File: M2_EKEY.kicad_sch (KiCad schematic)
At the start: 36 parts, among them J2 Bus_M.2_Socket_E, J31 Bus_M.2_Socket_E, J34 Bus_M.2_Socket_E

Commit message: went back to the drawing board
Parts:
- C200, C201, C202, C203, C49, C50, J34, R142, R148, R149, R150: now not fitted

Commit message: some power stuff (unfinished)
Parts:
- C200, C201, C202, C203, C49, C50, J34, R142, R148, R149, R150: now fitted
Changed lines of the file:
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@@
 		(exclude_from_sim no)
 		(in_bom yes)
-		(on_board no)
+		(on_board yes)
 		(in_pos_files yes)
-		(dnp yes)
+		(dnp no)
 		(property "Reference" "C203"
 			(at 228.6 173.99 90)
@@
 		(exclude_from_sim no)
 		(in_bom yes)
-		(on_board no)
+		(on_board yes)
 		(in_pos_files yes)
-		(dnp yes)
+		(dnp no)
 		(fields_autoplaced yes)
 		(property "Reference" "#PWR0292"
@@
 		(exclude_from_sim no)
 		(in_bom yes)
-		(on_board no)
+		(on_board yes)
 		(in_pos_files yes)
-		(dnp yes)
+		(dnp no)
 		(fields_autoplaced yes)
 		(property "Reference" "#PWR0289"
@@
 		(exclude_from_sim no)
 		(in_bom yes)
-		(on_board no)
+		(on_board yes)
 		(in_pos_files yes)
-		(dnp yes)
+		(dnp no)
 		(property "Reference" "C201"
 			(at 228.6 161.29 90)
@@
 		(exclude_from_sim no)
 		(in_bom yes)
-		(on_board no)
+		(on_board yes)
 		(in_pos_files yes)
-		(dnp yes)
+		(dnp no)
 		(property "Reference" "C49"
 			(at 156.21 193.04 90)
@@
 		(exclude_from_sim no)
 		(in_bom yes)
-		(on_board no)
+		(on_board yes)
 		(in_pos_files yes)
-		(dnp yes)
+		(dnp no)
 		(property "Reference" "C200"
 			(at 228.6 154.94 90)
@@
 		(exclude_from_sim no)
 		(in_bom yes)
-		(on_board no)
+		(on_board yes)
 		(in_pos_files yes)
-		(dnp yes)
+		(dnp no)
 		(property "Reference" "R148"
 			(at 264.16 256.54 90)
@@
 		(exclude_from_sim no)
 		(in_bom yes)
-		(on_board no)
+		(on_board yes)
 		(in_pos_files yes)
-		(dnp yes)
+		(dnp no)
 		(property "Reference" "R149"
 			(at 257.81 201.93 0)
@@
 		(exclude_from_sim no)
 		(in_bom yes)
-		(on_board no)
+		(on_board yes)
 		(in_pos_files yes)
-		(dnp yes)
+		(dnp no)
 		(fields_autoplaced yes)
 		(property "Reference" "#PWR0298"
@@
 		(exclude_from_sim no)
 		(in_bom yes)
-		(on_board no)
+		(on_board yes)
 		(in_pos_files yes)
-		(dnp yes)
+		(dnp no)
 		(fields_autoplaced yes)
 		(property "Reference" "J34"
@@
 		(exclude_from_sim no)
 		(in_bom yes)
-		(on_board no)
+		(on_board yes)
 		(in_pos_files yes)
-		(dnp yes)
+		(dnp no)
 		(fields_autoplaced yes)
 		(property "Reference" "#PWR0290"
@@
 		(exclude_from_sim no)
 		(in_bom no)
-		(on_board no)
+		(on_board yes)
 		(in_pos_files yes)
 		(dnp yes)
@@
 		(exclude_from_sim no)
 		(in_bom yes)
-		(on_board no)
+		(on_board yes)
 		(in_pos_files yes)
-		(dnp yes)
+		(dnp no)
 		(property "Reference" "R142"
 			(at 191.77 167.64 0)
@@
 		(exclude_from_sim no)
 		(in_bom yes)
-		(on_board no)
+		(on_board yes)
 		(in_pos_files yes)
-		(dnp yes)
+		(dnp no)
 		(property "Reference" "R150"
 			(at 264.16 204.47 0)
@@
 		(exclude_from_sim no)
 		(in_bom yes)
-		(on_board no)
+		(on_board yes)
 		(in_pos_files yes)
-		(dnp yes)
+		(dnp no)
 		(fields_autoplaced yes)
 		(property "Reference" "#PWR0291"
@@
 		(exclude_from_sim no)
 		(in_bom yes)
-		(on_board no)
+		(on_board yes)
 		(in_pos_files yes)
-		(dnp yes)
+		(dnp no)
 		(property "Reference" "C50"
 			(at 156.21 195.58 90)
@@
 		(exclude_from_sim no)
 		(in_bom yes)
-		(on_board no)
+		(on_board yes)
 		(in_pos_files yes)
-		(dnp yes)
+		(dnp no)
 		(property "Reference" "C202"
 			(at 228.6 167.64 90)

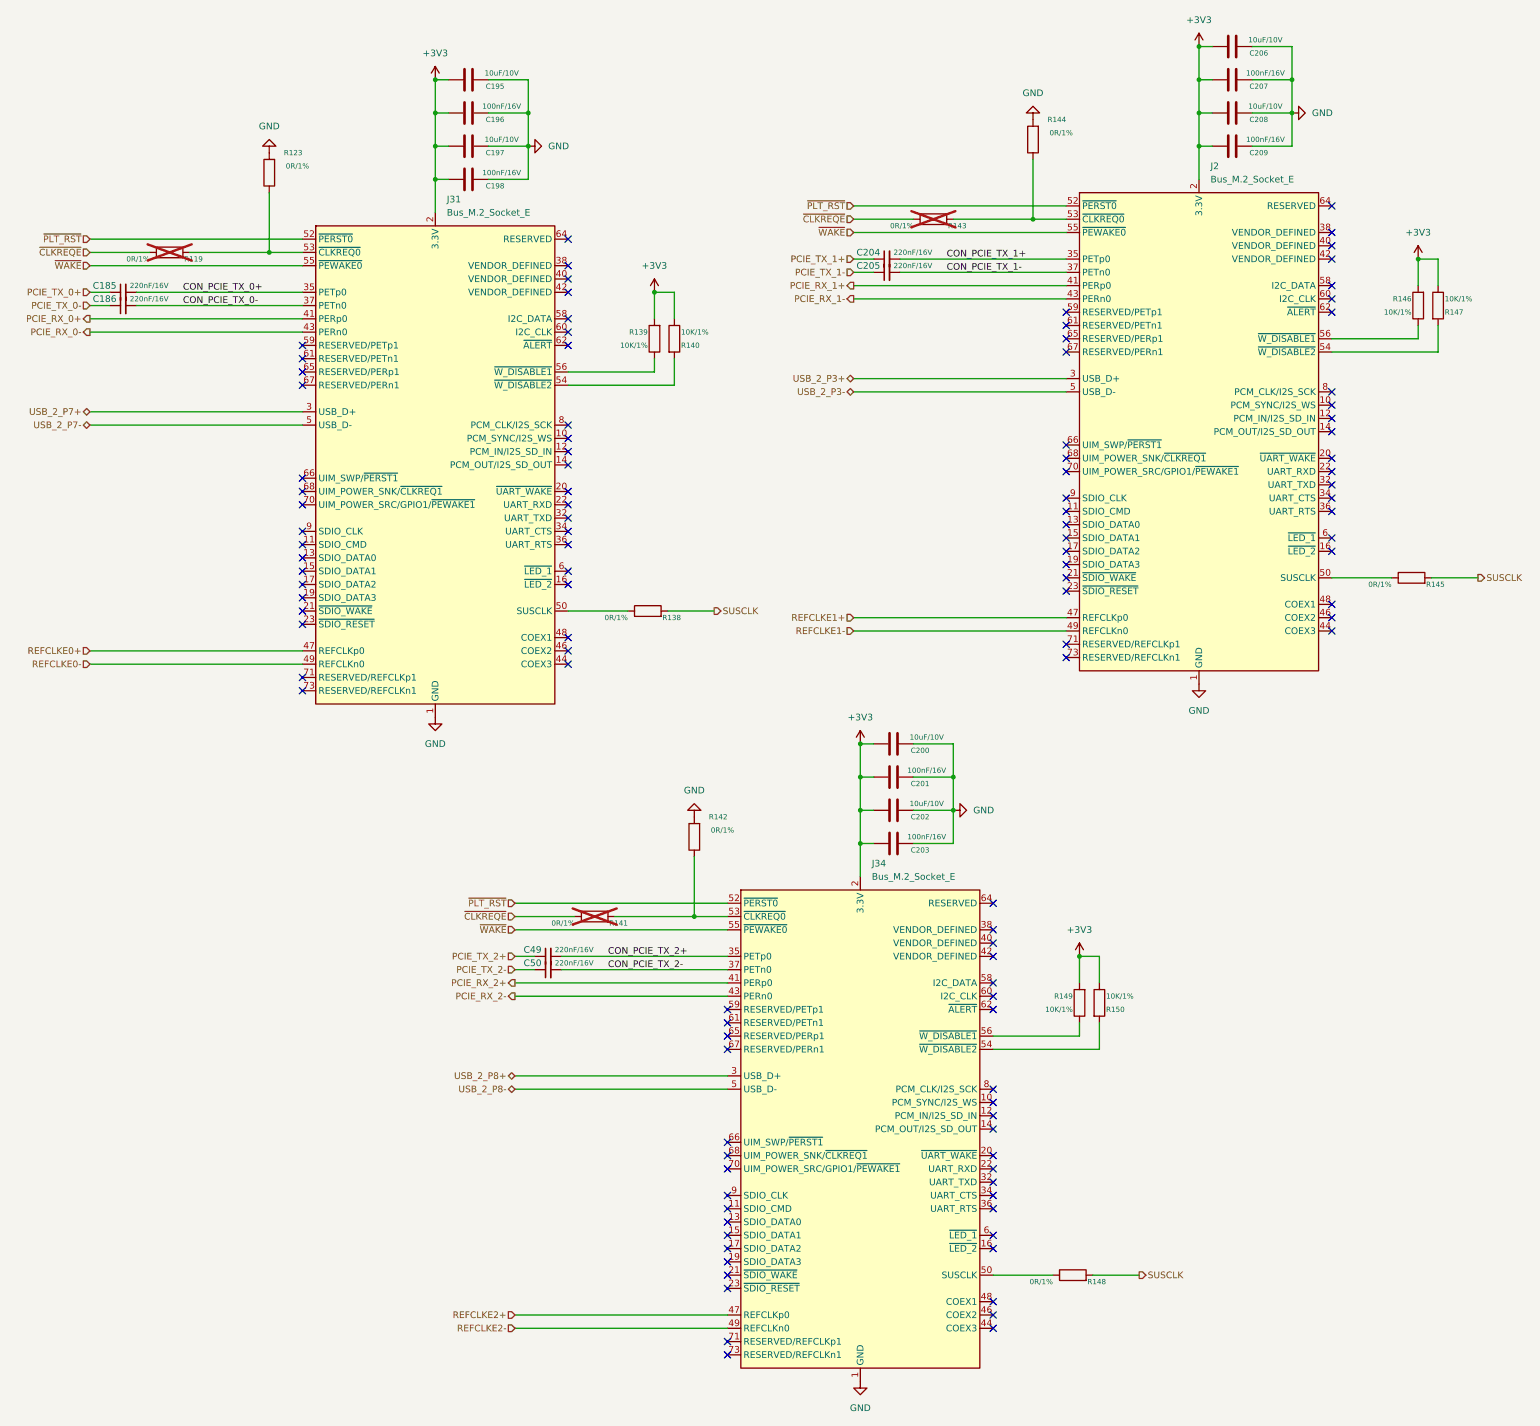
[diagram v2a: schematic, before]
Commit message: fixed 5v->3v bug
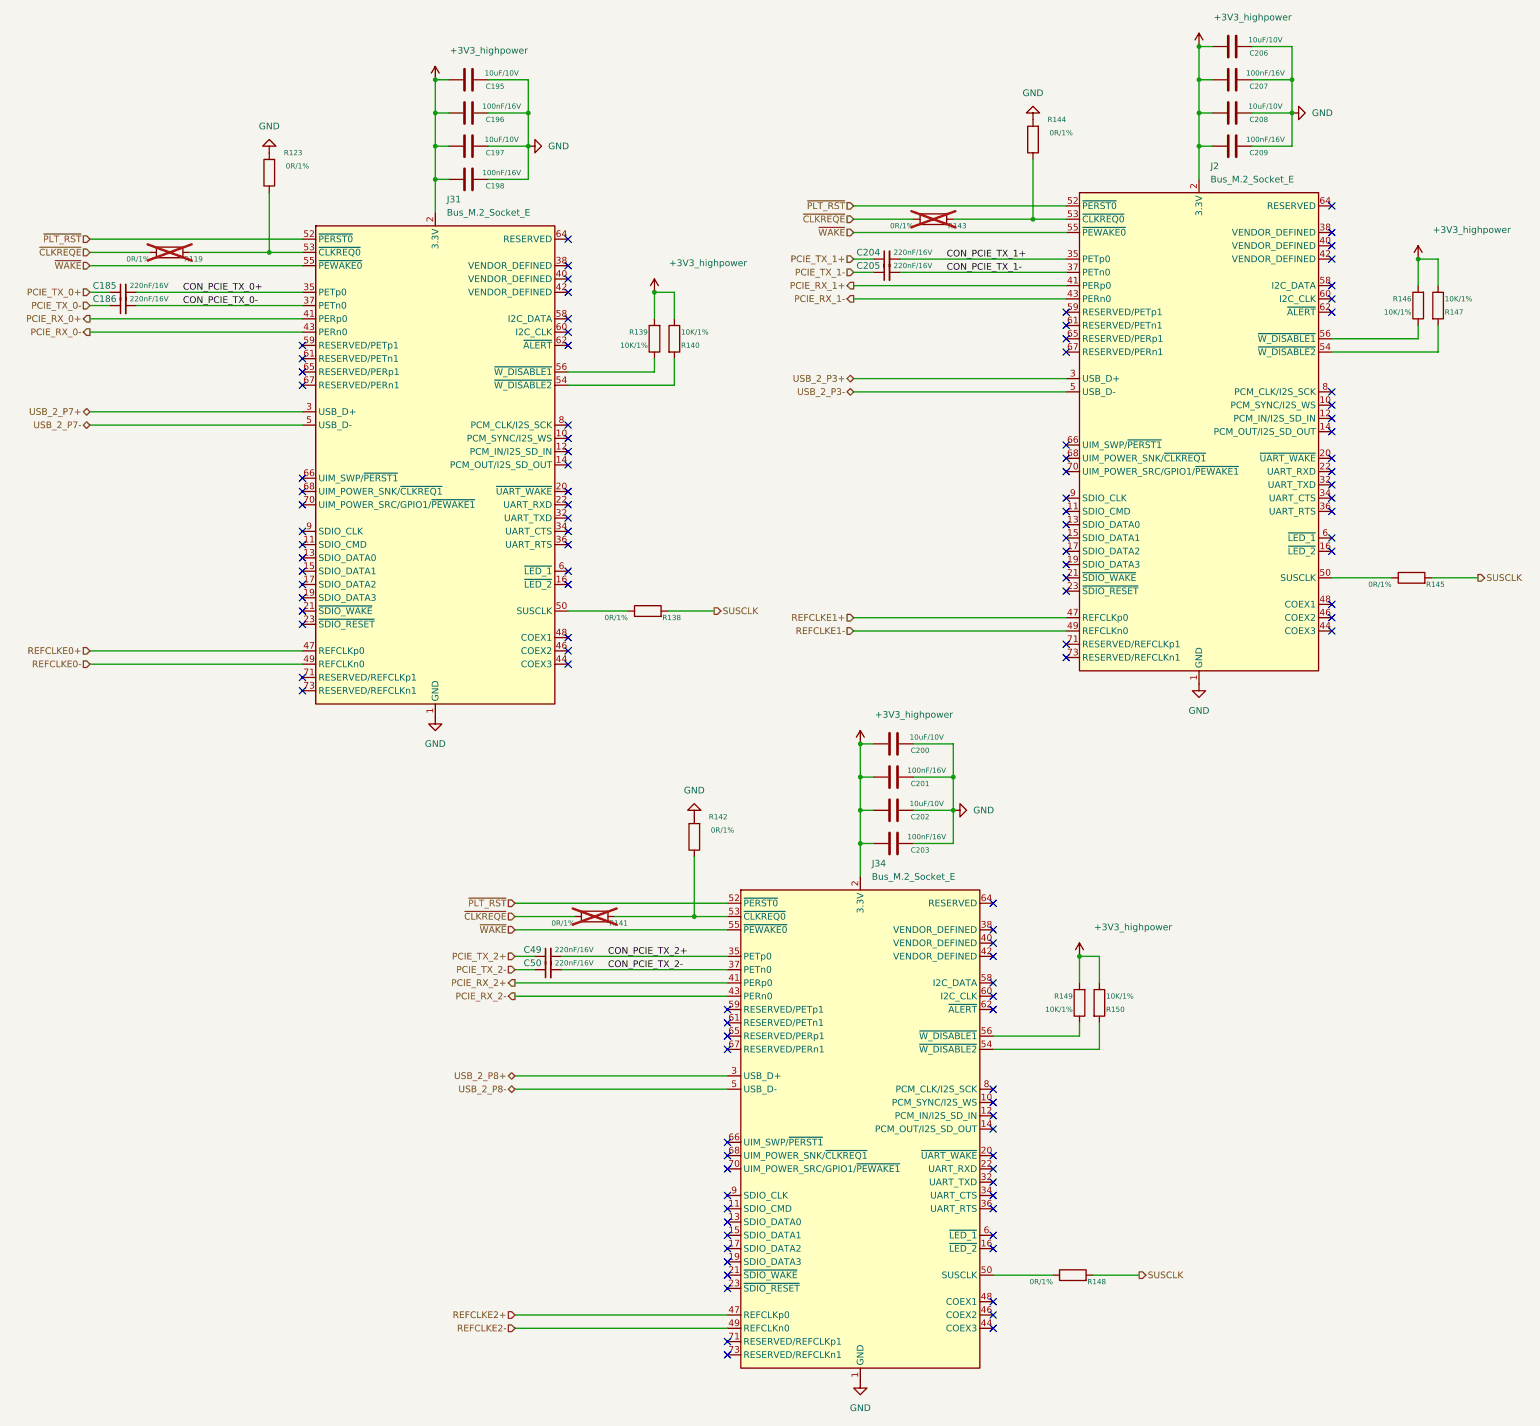
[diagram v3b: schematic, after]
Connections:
- net +3V3 renamed +3V3_highpower

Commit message: all power, diff pairs done, all components placed (final spot?) just some small wires left to route
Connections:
- net +3V3_highpower: now also C198.1; no longer C198.2
- net GND: now also C198.2; no longer C198.1
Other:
- moved on the sheet: C198
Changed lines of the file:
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@@
 	(symbol
 		(lib_id "Device:C")
-		(at 142.24 45.72 270)
+		(at 142.24 45.72 90)
+		(mirror x)
 		(unit 1)
 		(body_style 1)
@@
 		(dnp no)
 		(property "Reference" "C198"
-			(at 147.32 46.99 90)
+			(at 137.16 46.99 90)
 			(show_name no)
 			(do_not_autoplace no)
@@
 		)
 		(property "Value" "100nF/16V"
-			(at 148.59 44.45 90)
+			(at 135.89 44.45 90)
 			(show_name no)
 			(do_not_autoplace no)
@@
 		)
 		(property "Footprint" "A_HDJ_Library:C_0402_1005Metric"
-			(at 138.43 46.6852 0)
+			(at 146.05 46.6852 0)
 			(hide yes)
 			(show_name no)

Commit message: V4 done ???
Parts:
- added H10, H11, H6, H7, H8, H9: MountingHole_M2.0, MountingHole:MountingHole_2.7mm_Pad_TopOnly, symbol Mechanical:MountingHole_Pad
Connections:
- net GND: now also H10.1, H11.1, H6.1, H7.1, H8.1, H9.1

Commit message: last push before editing with the grid view (gonna break everything)
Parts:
- C185, C186: value 220nF/16V -> 220n; DF_Comment 贴片电容0402-220nF-16V-X7R -> (none); MPN (none) -> GCM155R71C224KE02D
- C195, C197, C200, C202, C206, C208: value 10uF/10V -> 10u; MPN (none) -> MLASL168BB5106MTNB33
- C204, C205, C49, C50: value 220nF/16V -> 220n; MPN (none) -> GCM155R71C224KE02D
- H10, H11, H9: now left out of the parts list
- R123, R142, R144: value 0R/1% -> 0; DF_Comment 贴片电阻0402-0R-1% -> (none); MPN (none) -> MCS0402HZ0000ZE100
- R138, R145: value 0R/1% -> 0; MPN (none) -> C2889341
- R139, R140, R149, R150: value 10K/1% -> 10K; MPN (none) -> RC0402FR-1310KL
- R146, R147: value 10K/1% -> 10K; DF_Comment 贴片电阻0402-10K-1% -> (none); MPN (none) -> RC0402FR-1310KL
- R148: value 0R/1% -> 0; DF_Comment 贴片电阻0402-0R-1% -> (none); MPN (none) -> C2889341
